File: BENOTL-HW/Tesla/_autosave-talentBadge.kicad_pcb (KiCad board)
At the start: 2 copper layers, 93.3 x 102.5 mm, 64 parts, among them P1 USB_A, P2 OLED, P3 Batt, P4 PS, P5 sd_card_spi, Q1 MMBT3904, Q2 MMBT3904, Q3 IR phototransistor, SW1 B1, SW2 B2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

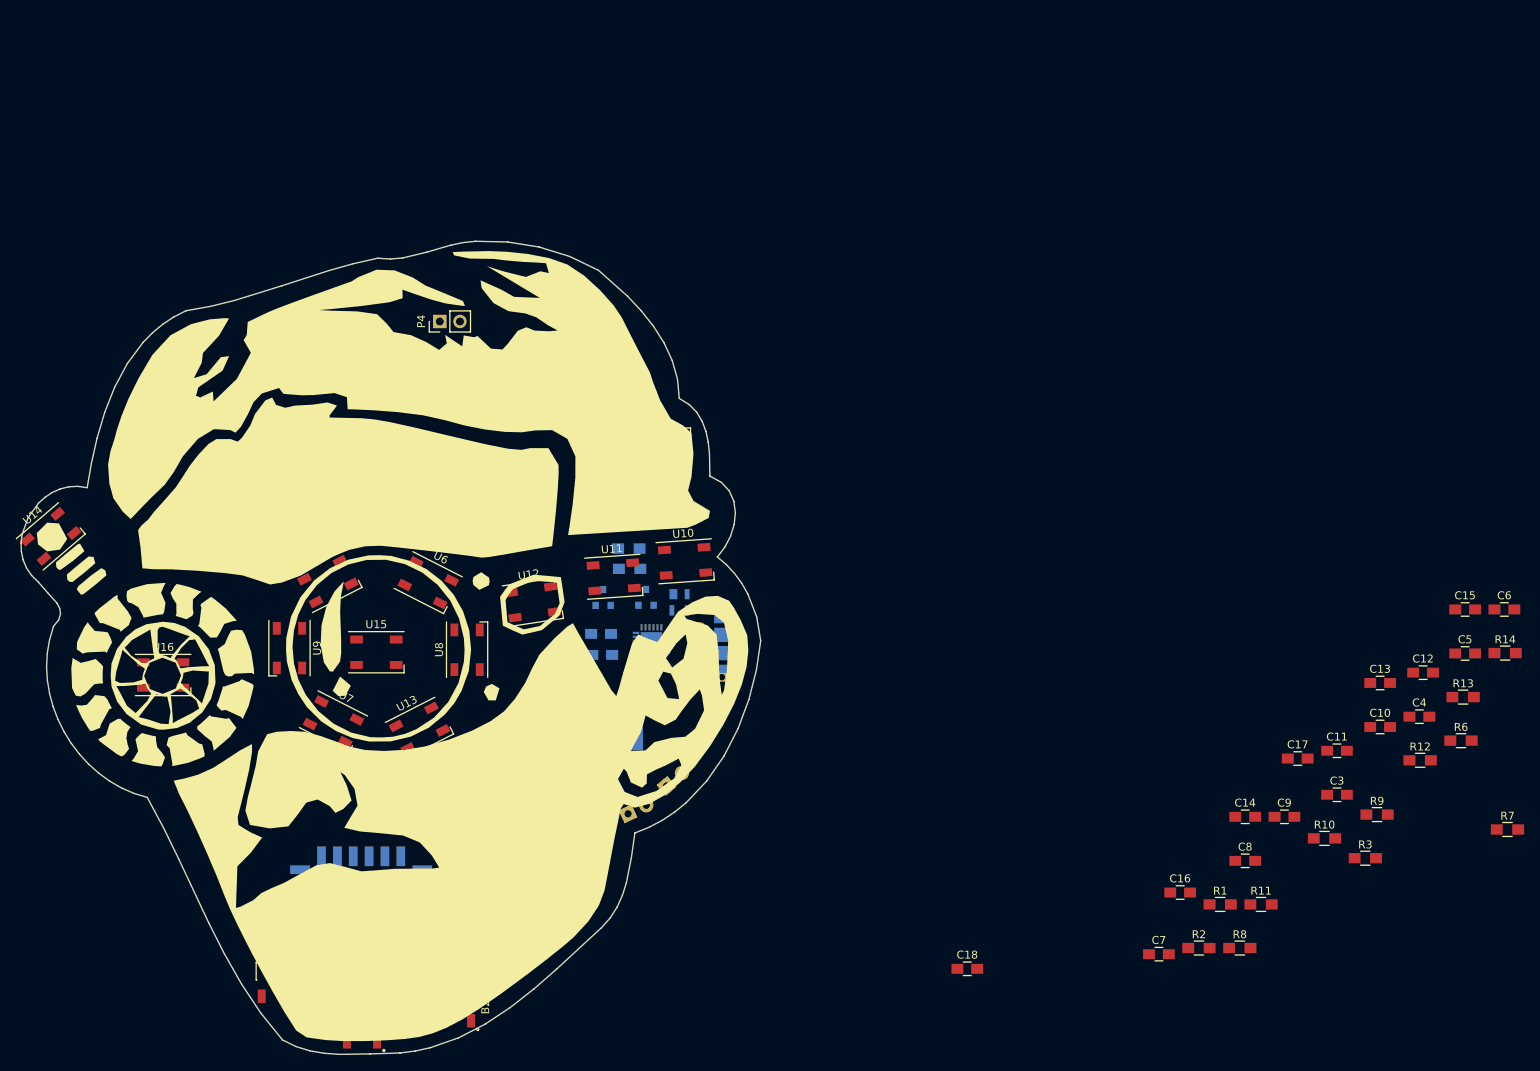
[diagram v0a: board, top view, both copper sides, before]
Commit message: Actualizado acomodo de footprints
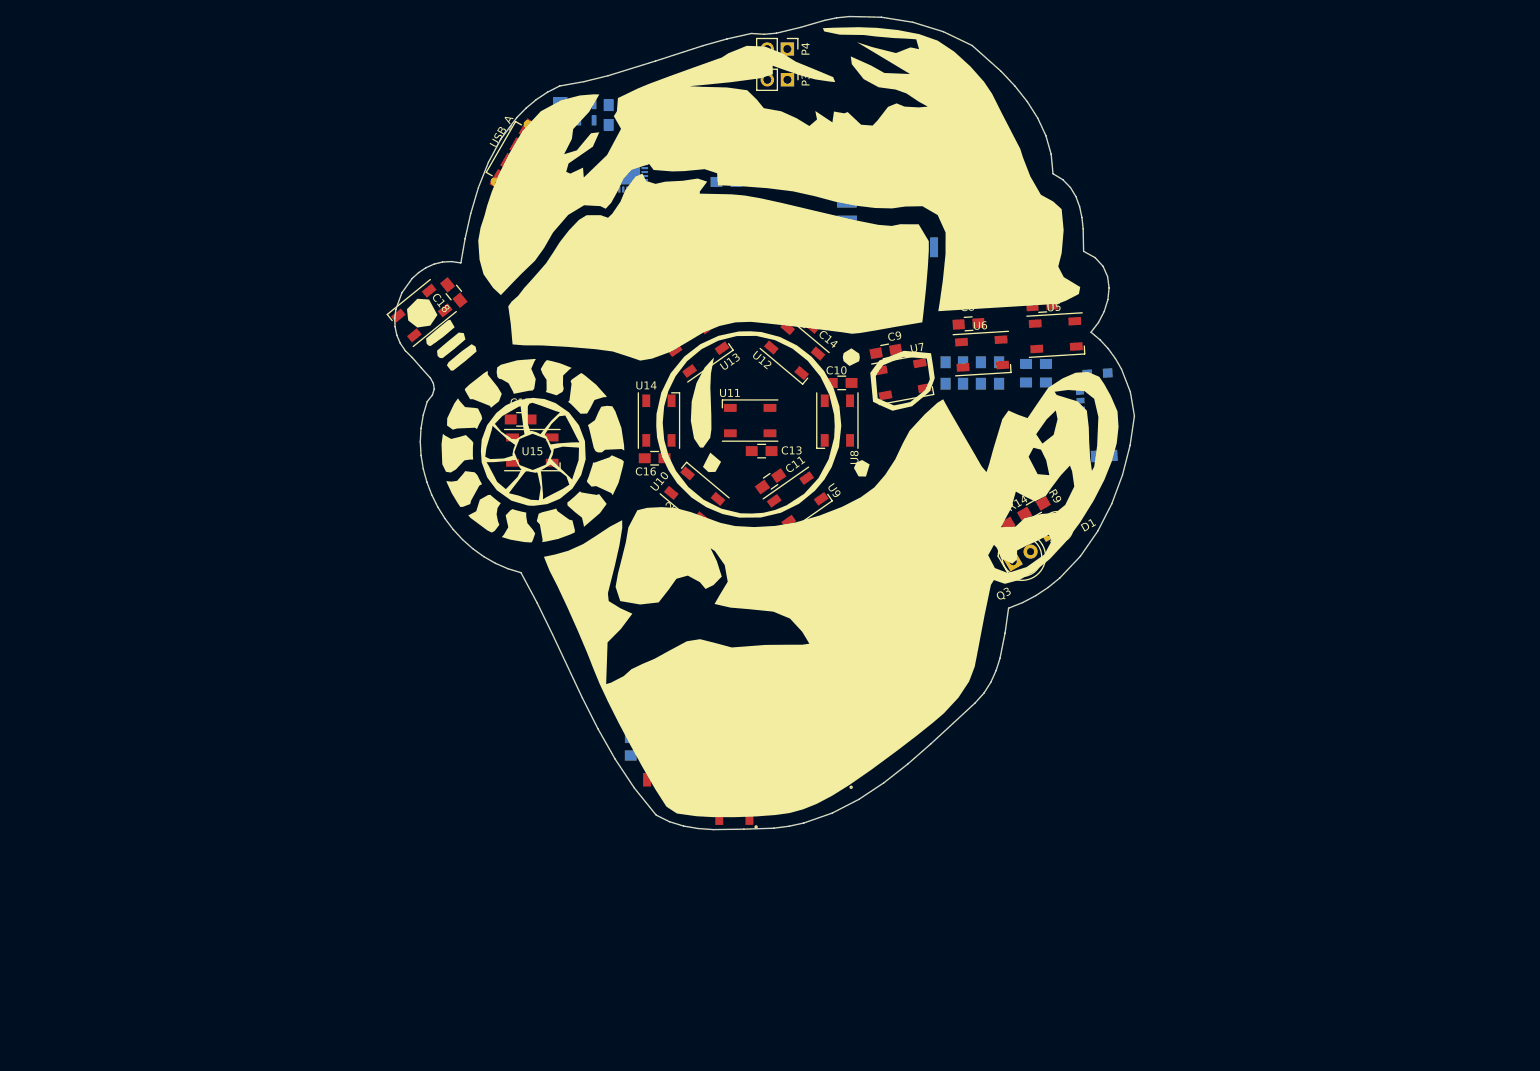
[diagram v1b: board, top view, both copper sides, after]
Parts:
- C3, C4, C5, C6, R1, R10, R11, R12, R13, R2, R3, R6, R7, R8: moved to B.Cu
- D1, P1, Q3: moved to F.Cu
- U1: footprint talentBadge:ESP-12E_SMD -> talentBadge:esp8266-12
- moved U1 119.9 mm to (137.2, 58.1), turned to 180 degrees
- moved C3 116.3 mm to (114.0, 40.0)
- moved C4 110.4 mm to (114.0, 49.9), turned to 180 degrees
- moved R7 109.8 mm to (103.3, 120.0), turned to 180 degrees
- moved C18 107.1 mm to (79.6, 63.9), turned to 129 degrees
- moved C17 106.9 mm to (88.0, 79.8)
- moved C15 106.0 mm to (107.1, 68.7), turned to 35 degrees
- moved R3 105.5 mm to (125.0, 56.0), turned to 90 degrees
- moved R2 104.1 mm to (122.5, 55.9), turned to 90 degrees
- moved R6 103.4 mm to (103.3, 117.8), turned to 180 degrees
- moved U5 96.9 mm to (155.5, 69.2), turned to 3.5 degrees
- moved R1 96.6 mm to (150.2, 48.0), turned to 270 degrees
- moved P5 96.0 mm to (160.2, 79.3), turned to 273.5 degrees
- moved C12 95.0 mm to (108.7, 93.4), turned to 140 degrees
- moved C16 86.0 mm to (105.0, 84.8)
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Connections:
- U3 pad 3: Net-(P1-Pad3) -> Net-(P1-Pad2)
- U3 pad 4: Net-(P1-Pad2) -> Net-(P1-Pad3)
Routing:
- net Net-(Q1-Pad1): track 0.00 -> 4.59 mm
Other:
- net class Default: trace_width 0.25 -> 0.4; via_dia 0.6 -> 0.8; via_drill 0.4 -> 0.6
- net class Vcc added: clearance 0.4, trace_width 1, via_dia 1.2, via_drill 0.6
